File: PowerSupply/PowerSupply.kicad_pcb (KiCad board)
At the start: 2 copper layers, 39 x 30 mm, 15 parts, among them J1 POWER, J2 VSET, J3 LASER, U0 AL8861Y-13

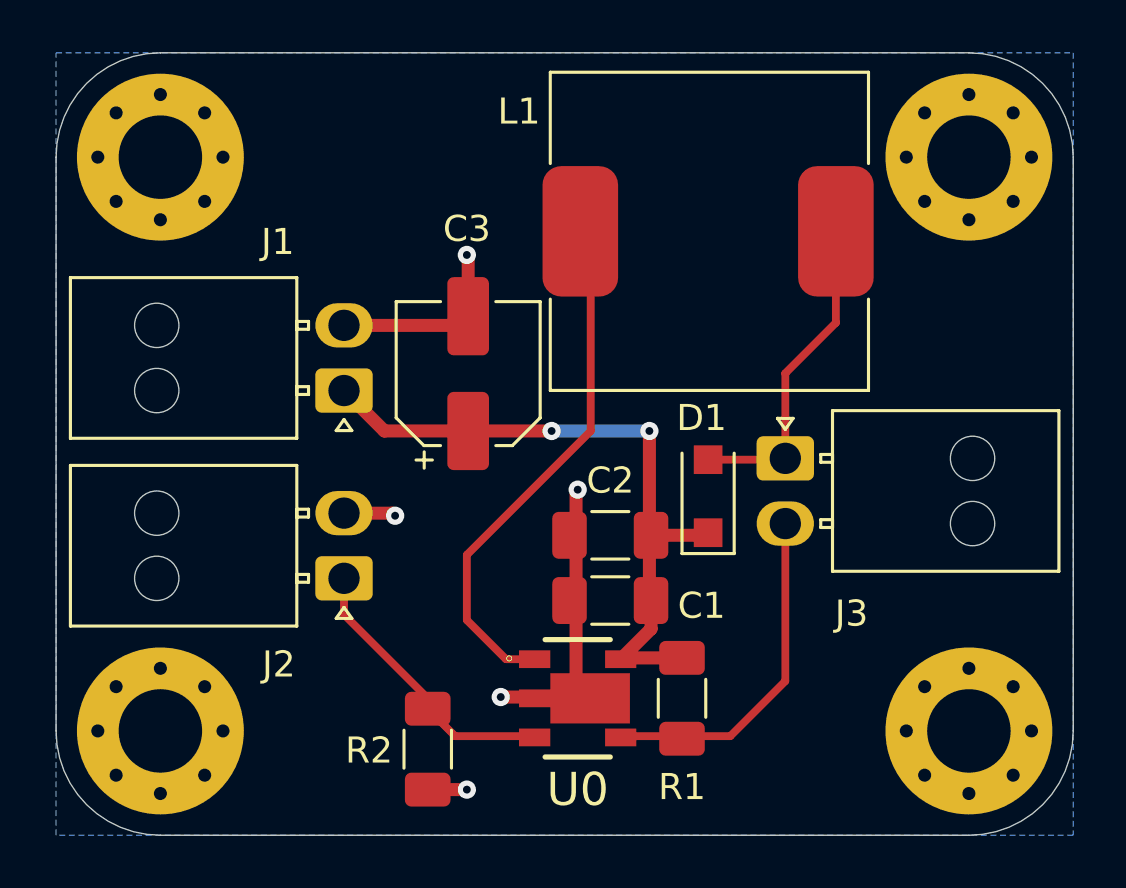
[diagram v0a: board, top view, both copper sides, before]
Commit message: Prepare version for manufacturing: finalize PCB layout, add silkscreen
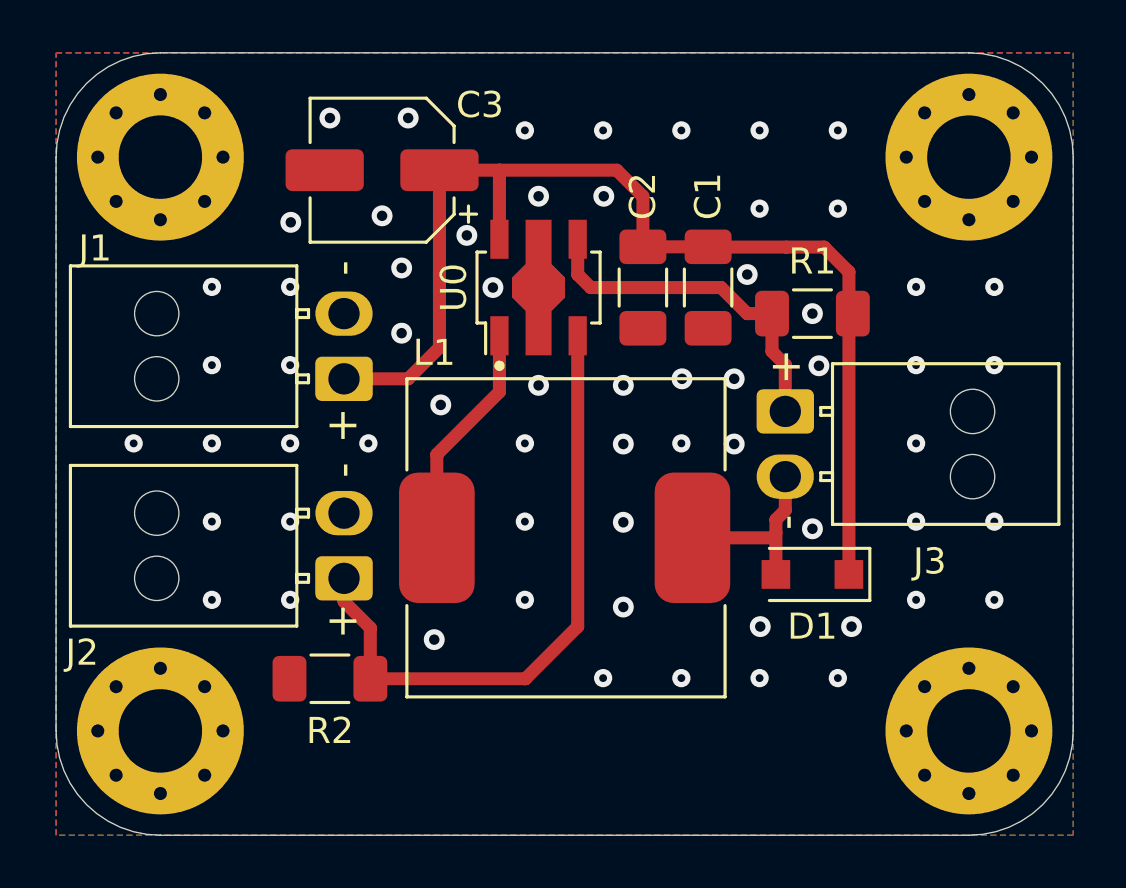
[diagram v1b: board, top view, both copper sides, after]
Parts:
- added kibuzzard-630BEA7A: G***, kibuzzard-630BEA7A, B.Cu at (162.5, 85.0)
- added kibuzzard-630BEA96: G***, kibuzzard-630BEA96, B.Cu at (126.8, 89.0)
- added kibuzzard-630BEA9F: G***, kibuzzard-630BEA9F, B.Cu at (126.8, 81.2)
- U0: footprint SamacSys_Parts:SOT89-5 -> Package_TO_SOT_SMD:SOT-89-5
- moved U0 15.8 mm to (143.5, 79.0), turned to 90 degrees
- moved R1 15.6 mm to (154.0, 80.0), turned to 180 degrees
- moved L1 13.0 mm to (138.4, 82.5)
- moved C1 12.6 mm to (150.0, 79.0), turned to -90 degrees
- moved C2 9.58 mm to (147.5, 79.0), turned to -90 degrees
- moved C3 8.47 mm to (137.5, 74.5), turned to 180 degrees
- moved D1 5.00 mm to (154.0, 90.0), turned to 180 degrees
- moved R2 4.62 mm to (135.5, 94.0), turned to 180 degrees
- moved J3 1.80 mm to (153.0, 83.8)
- moved J1 0.45 mm to (136.0, 82.5)
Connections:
- D1 pad 2: Net-(J3-Pad1) -> Net-(D1-Pad2)
- J3 pad 1: Net-(J3-Pad1) -> /ISENSE
- J3 pad 2: /ISENSE -> Net-(D1-Pad2)
- L1 pad 2: Net-(J3-Pad1) -> Net-(D1-Pad2)
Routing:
- net GND: track 20.2 -> 0.00 mm, vias 5 -> 62
- net +5V: track 26.0 -> 43.2 mm, vias 2 -> 0
- net /VSET: track 10.9 -> 24.2 mm
- net Net-(J3-Pad1): track 12.2 -> 0.00 mm
- net Net-(L1-Pad1): track 20.3 -> 8.74 mm
- net Net-(D1-Pad2): track 0.00 -> 7.00 mm
- added copper zone on F.Cu, net GND
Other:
- board text added: "+"
- board text added: "-"
- board text added: "Profilometry - Laser diode driver Designed by: Prochazka & Malanik 08/2022 - v0.1 - STRaDe @ VUT FIT"
- board text removed: "Ideální je mít GND plane na obou vrstvách Stačí v nastaveí plane vybrat i druhou vrstvu"
- board text removed: "Ideální je na desku přidat i popisek (vrstva silkscreen) s datem, verzí, o co se jedná a kdo je autor"
- board text removed: "Neni nutne mit extra tenke cesty, klidně by zde vsiude mohlo být 0.5mm"
- board text removed: "Pokud je to možné použijte standardní footprint Tento konkrétní v knihovnách kicadu je: Doporučuji minimálně stahovat, radši si to nakreslete sám pak neskončíte s nekvalitními footprinty Tento zrovna není ideální, z knihovny: Package_TO_SOT_SMD:SOT-89-5"
- board text removed: "Při updatu PCB ze schematu jsou nejake chyby stejne tak ERC ukazuje varování Ještě jednou poznamenávám že než mi to pošlete na review meli by vsechny kontroly ukazovat 0 chyba 0 varování Konkrétně ERC, update PCB ze schematu, DRC"
- board text removed: "Spínací cesta by měla být co nejkratší kvůli rušení a zpětné vazbě, vy ji máte nejdelší Doporučuji shlédnout: https://www.youtube.com/watch?v=AmfLhT5SntE Je to obdobné reší spínaný regulátor, což je téměř identické. Tento konkrétné obvod neumoznuje uplne ideální zapojení nicméně slo by to o hodně zlepsit"
- board text removed: "Tento prokov je zbytečný Prokovení je způsobeno už uchycením THT součástky zde V případě GND plochy na obou stranách by neměl už vůbec cenu Má cenu ovšem prokovit dvě GND plochy mezi sebou (vis stitching) Stitching je vhodný pro návratové proudy a tepelnou distribuci Plugin: https://github.com/jsreynaud/kicad-action-scripts nebo https://github.com/weirdgyn/viastitching"
- board text removed: "Titulní blok"
- board text removed: "U konektoru by měl být popisek k čemu jsou a jaké je jejih polarita Usnadní to ozivovaní a použivani"
- board text removed: "Z plosek se snazte jit pokud mozno kolmo na jejich tvar Ma to zase vliv na ruseni a u desek s uzsimi cesty i na jejich vyrobitelnost"
